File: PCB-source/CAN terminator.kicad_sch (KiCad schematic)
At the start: 3 parts, among them SW5 SW_DIP_x02

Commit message: vrm VIP
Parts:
- removed R24, R39: 120R, Resistor_SMD:R_0603_1608Metric, symbol Device:R
- added Q2, Q3, Q5, Q6: AO3400A, PCM_JLCPCB:Q_SOT-23, symbol PCM_JLCPCB-Transistors:NMOS,AO3400A
- added R1, R2: 120Ω, PCM_JLCPCB:R_0402, symbol PCM_JLCPCB-Resistors:0402,120Ω
- added R3, R5: 10kΩ, PCM_JLCPCB:R_0402, symbol PCM_JLCPCB-Resistors:0402,10kΩ
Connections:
- net CAN1.+: now also SW5.2, R2.1; no longer SW5.4
- net CAN1.-: now also SW5.3, Q6.3 (D)
- net CAN2.+: now also SW5.1, R1.1
- net CAN2.-: now also SW5.4, Q3.3 (D); no longer SW5.3
- new net: Q5.2 (S), Q6.2 (S)
- new net: Q5.3 (D), R2.2
- new net: Q2.2 (S), Q3.2 (S)
- new net: Q2.3 (D), R1.2
- new net CAN_AUTOTERM.1: Q5.1 (G), Q6.1 (G), R3.1
- new net CAN_AUTOTERM.2: Q2.1 (G), Q3.1 (G), R5.1
- new net GND: R3.2, R5.2
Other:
- note added: "Artem H."
- note added: "Autoterminator CAN"
- note removed: "CAN BUS TERMINATOR"
- note removed: "Terminator"
- moved on the sheet: SW5

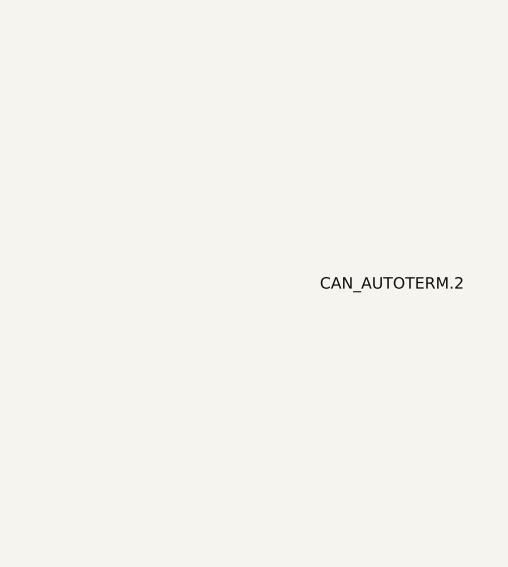
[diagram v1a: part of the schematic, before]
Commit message: Finish component and diffpair placement
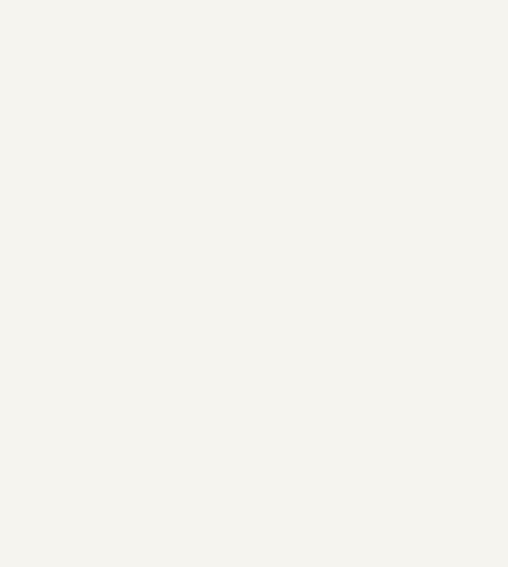
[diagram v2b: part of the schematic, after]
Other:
- title: MMS2 -> CAN Auto terminator
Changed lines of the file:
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@@
 	(paper "A4")
 	(title_block
-		(title "MMS2")
+		(title "CAN Auto terminator")
 		(date "2025-04-22")
 		(rev "A")
@@
 		(effects
 			(font
-				(size 1.27 1.27)
-				(thickness 0.1588)
-			)
-			(justify left bottom)
-		)
-	)
-	(label "CAN_AUTOTERM.2"
-		(at 336.55 104.14 0)
-		(effects
-			(font

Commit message: in progress
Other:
- note added: "NOTE:"
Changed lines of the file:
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@@
+		)
+	)
+	(text "NOTE:"
+		(exclude_from_sim no)
+		(at 101.092 130.302 0)
+		(effects
+			(font
+				(size 2.54 2.54)
+				(thickness 0.254)
+				(bold yes)
+			)
 		)
 	)
